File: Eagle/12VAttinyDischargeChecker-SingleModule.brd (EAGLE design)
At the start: 121.6 x 70.4 mm, 82 parts

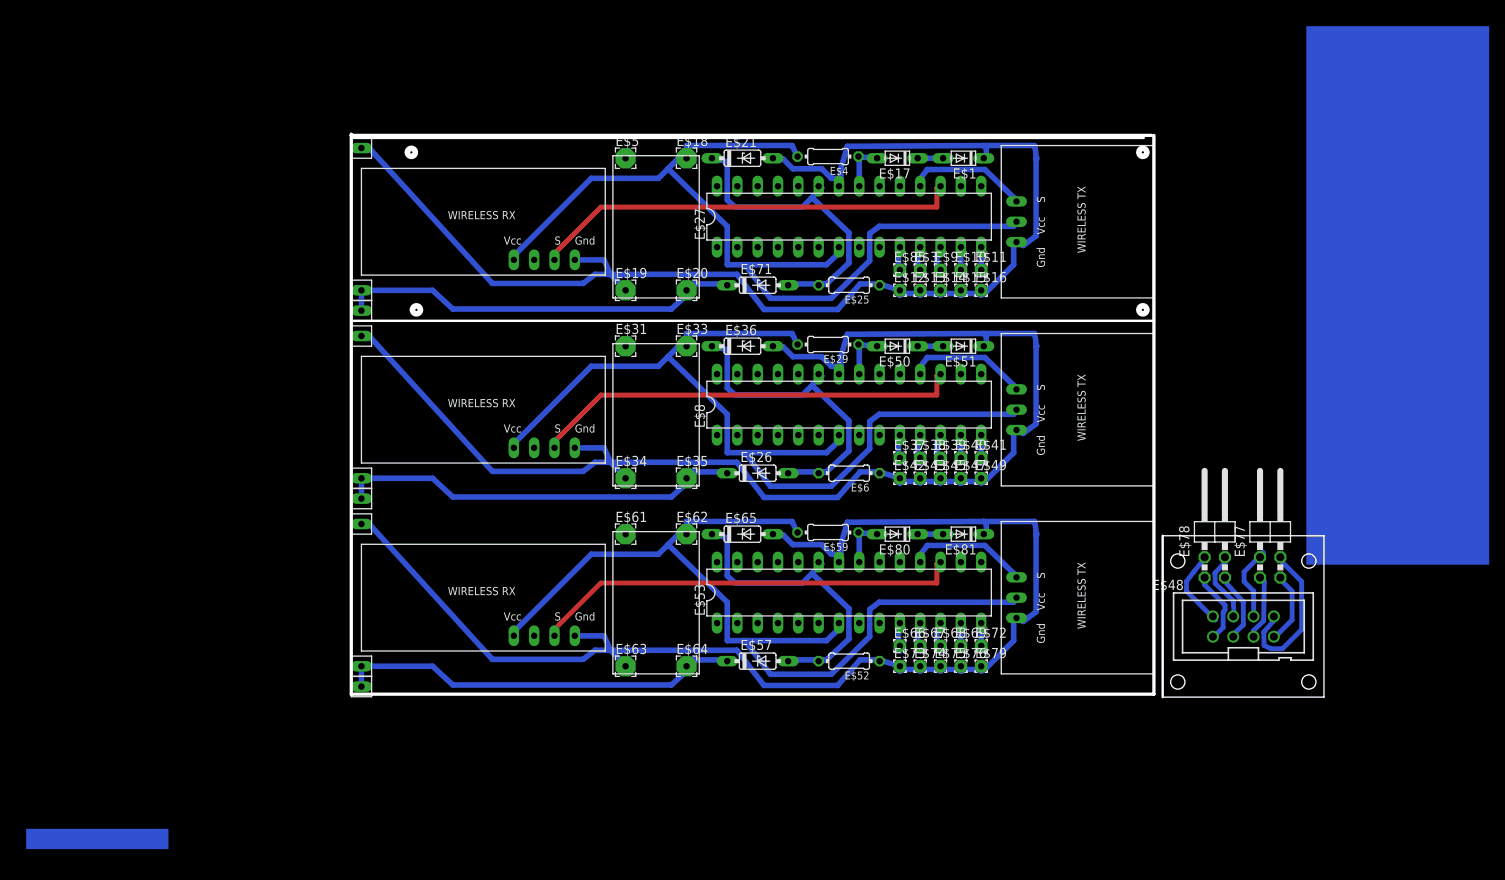
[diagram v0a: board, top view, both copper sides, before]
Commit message: Aggiunti file controllo e modifica al circuito single module per aggiungere debug e altre modifiche
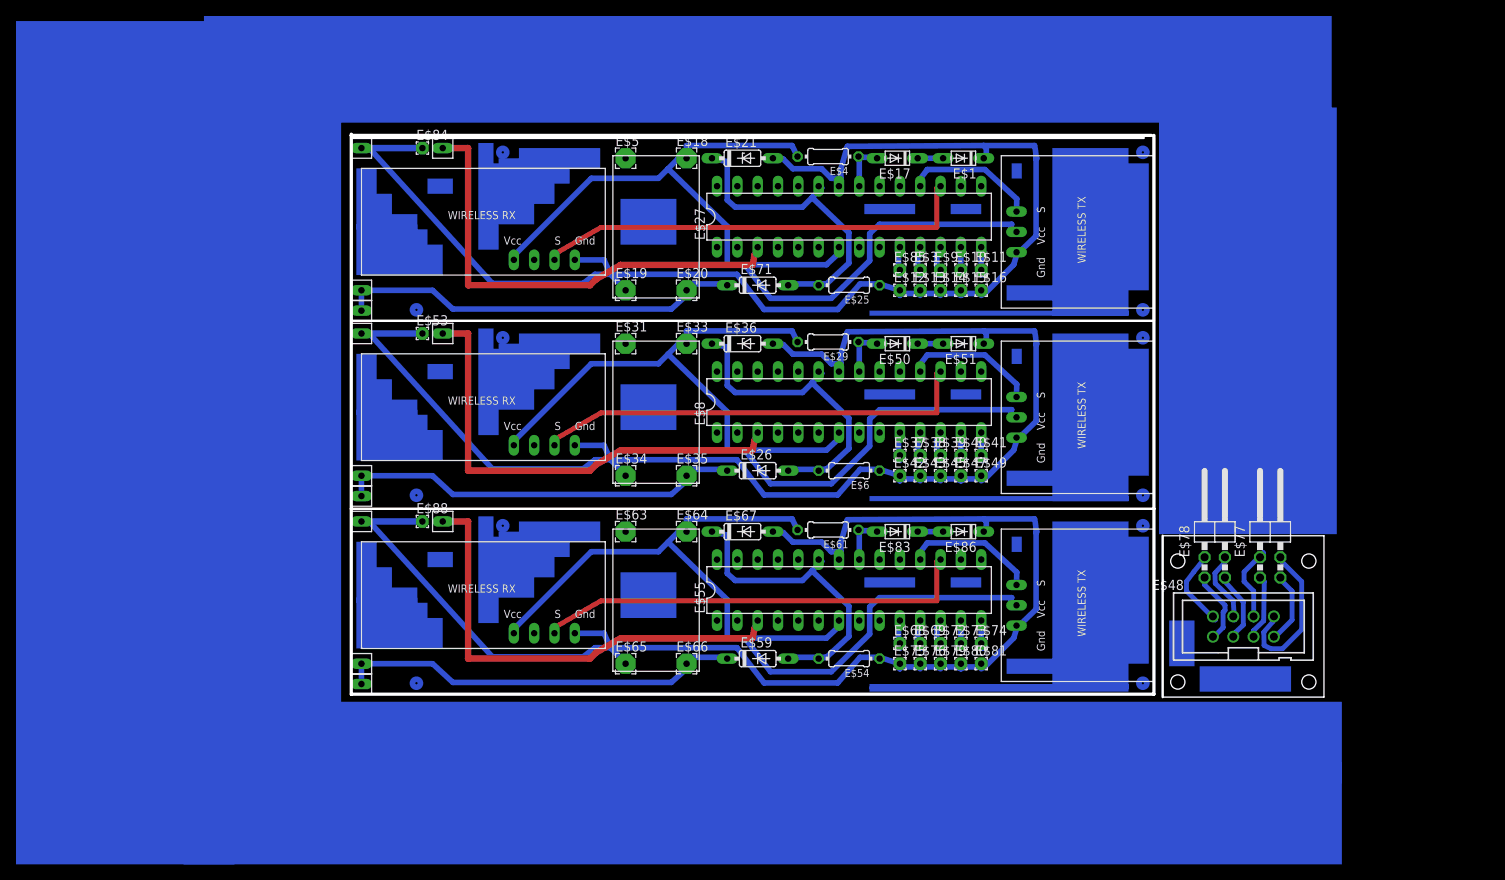
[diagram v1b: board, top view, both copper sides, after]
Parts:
- added E$82, E$87: (no value), con-lsta2:FE01-1
- added E$83, E$86: (no value), diode:DO34-5
- added E$84, E$88: (no value), wirepad:1,6/0,8
- E$52: value 220 -> (none); device eagle-ltspice:0204/7 -> con-lsta2:FE01-1
- E$53: device 74xx-us:DIL28-3 -> wirepad:1,6/0,8
- E$54: value (none) -> 220; device LSGPackages:WIRELESS-TX-FLAT -> eagle-ltspice:0204/7
- E$55: device con-lsta2:FE01-1 -> 74xx-us:DIL28-3
- E$56: device con-lsta2:FE01-1 -> LSGPackages:WIRELESS-TX-FLAT
- E$57: value Zener 12v -> (none); device ref-packages:DO35Z7 -> con-lsta2:FE01-1
- E$58: device LSGPackages:WIRELESS-RX-FLAT -> con-lsta2:FE01-1
- E$59: value 220 -> Zener 12v; device eagle-ltspice:0204/7 -> ref-packages:DO35Z7
- E$60: device con-lsta2:FE01-1 -> LSGPackages:WIRELESS-RX-FLAT
- E$61: value (none) -> 220; device wirepad:2,54/0,8 -> eagle-ltspice:0204/7
- E$62: device wirepad:2,54/0,8 -> con-lsta2:FE01-1
- E$65: value Zener 5v -> (none); device ref-packages:DO35Z7 -> wirepad:2,54/0,8
- E$66: device wirepad:1,6/0,8 -> wirepad:2,54/0,8
- E$67: value (none) -> Zener 5v; device wirepad:1,6/0,8 -> ref-packages:DO35Z7
- E$80, E$81: device diode:DO34-5 -> wirepad:1,6/0,8
- moved E$56 88.7 mm to (89.5, 12.1)
- moved E$52 64.5 mm to (11.4, 44.1), turned to 270 degrees
- moved E$53 62.4 mm to (8.89, 45.4)
- moved E$55 61.9 mm to (62.2, 13.3), turned to 0 degrees
- moved E$57 49.6 mm to (1.27, 2.86), turned to 90 degrees
- moved E$62 40.7 mm to (1.27, 23.2), turned to 90 degrees
- moved E$54 28.5 mm to (62.2, 4.76), turned to 180 degrees
- moved E$66 26.8 mm to (41.9, 4.13)
- moved E$67 26.4 mm to (48.9, 20.6)
- moved E$61 25.3 mm to (59.6, 20.8), turned to 180 degrees
- moved E$65 21.8 mm to (34.3, 4.13)
- moved E$58 19.2 mm to (1.27, 2.86), turned to 270 degrees
- moved E$59 18.1 mm to (50.8, 4.76), turned to 0 degrees
- moved E$80 18.0 mm to (76.2, 4.13), turned to 0 degrees
- moved E$60 17.2 mm to (16.5, 14.9), turned to 0 degrees
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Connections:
- new net S$42: E$27.3, E$82.1
- new net S$45: E$83.C, E$86.A
- new net S$46: E$55.3, E$87.1
- net S$18: now also E$53.1; no longer E$30.1
- net S$28: now also E$52.1, E$8.3; no longer E$53.7, E$54.P$1, E$58.P$1, E$59.2, E$62.1
- net S$29: now also E$55.7, E$56.P$1, E$60.P$1, E$61.2; no longer E$55.1, E$56.1, E$57.C
- net S$30: now also E$57.1, E$58.1, E$59.C, E$66.1; no longer E$52.2, E$53.23, E$57.A, E$65.C
- net S$31: now also E$54.2, E$55.23, E$59.A, E$67.C; no longer E$52.1, E$53.22, E$54.P$3, E$58.P$4, E$60.1, E$63.1, E$65.A, E$81.C
- net S$32: now also E$54.1, E$55.22, E$56.P$3, E$60.P$4, E$65.1, E$67.A, E$86.C, E$88.1; no longer E$53.18, E$54.P$2
- net S$33: now also E$55.18, E$56.P$2; no longer E$53.21, E$59.1, E$80.A
- net S$34: now also E$55.21, E$61.1, E$83.A; no longer E$53.17, E$58.P$3
- net S$35: now also E$55.17, E$60.P$3; no longer E$53.14
- net S$36: now also E$55.14; no longer E$53.13
- net S$37: now also E$84.1
- net S$38: now also E$55.13; no longer E$53.12
- net S$39: now also E$55.12; no longer E$53.11
- net S$40: now also E$55.11; no longer E$53.10
- net S$41: now also E$55.10; no longer E$80.C, E$81.A
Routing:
- net S$32: track 15.2 -> 169.5 mm
- net S$31: track 163.0 -> 40.1 mm
- net S$29: track 51.2 -> 116.1 mm
- net S$46: track 0.00 -> 59.0 mm
- net S$42: track 0.00 -> 59.0 mm
- net S$28: track 115.8 -> 59.0 mm
- net S$35: track 4.04 -> 55.0 mm
- net S$34: track 54.0 -> 6.01 mm
- net S$30: track 40.1 -> 51.2 mm
- net S$33: track 6.01 -> 16.6 mm
- net S$37: track 163.0 -> 169.5 mm
- net S$18: track 163.0 -> 169.5 mm
- net S$45: track 0.00 -> 3.18 mm
- net S$16: track 15.2 -> 16.6 mm
- net S$19: track 15.2 -> 16.6 mm
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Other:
- outline, holes or cut-outs redrawn
- board text added: "debug"

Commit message: .
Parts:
- removed E$22, E$56: (no value), LSGPackages:WIRELESS-TX-FLAT
- removed E$23, E$24, E$30, E$52, E$57, E$58, E$62, E$87: (no value), con-lsta2:FE01-1
- removed E$26, E$59: Zener 12v, ref-packages:DO35Z7
- removed E$28, E$60: (no value), LSGPackages:WIRELESS-RX-FLAT
- removed E$29, E$54, E$6, E$61: 220, eagle-ltspice:0204/7
- removed E$31, E$33, E$34, E$35, E$63, E$64, E$65, E$66: (no value), wirepad:2,54/0,8
- removed E$36, E$67: Zener 5v, ref-packages:DO35Z7
- removed E$37, E$38, E$39, E$40, E$41, E$42, E$43, E$45, E$47, E$49, E$53, E$68, E$69, E$72, E$73, E$74, E$75, E$76, E$79, E$80, E$81, E$88: (no value), wirepad:1,6/0,8
- removed E$50, E$51, E$83, E$86: (no value), diode:DO34-5
- removed E$55, E$8: (no value), 74xx-us:DIL28-3
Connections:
- removed net S$13: E$22.P$1, E$28.P$1, E$29.2, E$33.1, E$8.7
- removed net S$14: E$23.1, E$24.1, E$26.C, E$35.1
- removed net S$17: E$26.A, E$36.C, E$6.2, E$8.23
- removed net S$18: E$22.P$3, E$28.P$4, E$34.1, E$36.A, E$51.C, E$53.1, E$6.1, E$8.22
- removed net S$19: E$22.P$2, E$8.18
- removed net S$20: E$29.1, E$50.A, E$8.21
- removed net S$21: E$28.P$3, E$8.17
- removed net S$22: E$8.14
- removed net S$23: E$8.13
- removed net S$24: E$8.12
- removed net S$25: E$8.11
- removed net S$26: E$8.10
- removed net S$27: E$50.C, E$51.A
- removed net S$28: E$52.1, E$8.3
- removed net S$29: E$55.7, E$56.P$1, E$60.P$1, E$61.2, E$64.1
- removed net S$30: E$57.1, E$58.1, E$59.C, E$66.1
- removed net S$31: E$54.2, E$55.23, E$59.A, E$67.C
- removed net S$32: E$54.1, E$55.22, E$56.P$3, E$60.P$4, E$65.1, E$67.A, E$86.C, E$88.1
- removed net S$33: E$55.18, E$56.P$2
- removed net S$34: E$55.21, E$61.1, E$83.A
- removed net S$35: E$55.17, E$60.P$3
- removed net S$36: E$55.14
- removed net S$38: E$55.13
- removed net S$39: E$55.12
- removed net S$40: E$55.11
- removed net S$41: E$55.10
- removed net S$45: E$83.C, E$86.A
- removed net S$46: E$55.3, E$87.1
- new net S$47: E$27.6, E$85.1
- net S$15: now also E$27.20
- net S$37: now also E$27.8
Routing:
- net S$32: track 169.5 -> 0.00 mm
- net S$18: track 169.5 -> 0.00 mm
- net S$13: track 116.1 -> 0.00 mm
- net S$29: track 116.1 -> 0.00 mm
- net S$28: track 59.0 -> 0.00 mm
- net S$46: track 59.0 -> 0.00 mm
- net S$35: track 55.0 -> 0.00 mm
- net S$21: track 55.0 -> 0.00 mm
- net S$30: track 51.2 -> 0.00 mm
- net S$14: track 51.2 -> 0.00 mm
- net S$31: track 40.1 -> 0.00 mm
- net S$17: track 40.1 -> 0.00 mm
- net S$47: track 0.00 -> 18.5 mm
- net S$33: track 16.6 -> 0.00 mm
- net S$19: track 16.6 -> 0.00 mm
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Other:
- outline, holes or cut-outs redrawn

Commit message: .
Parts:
- added E$22: (no value), LSGPackages:WIRELESS-TX-FLAT
- added E$23, E$24, E$30, E$52: (no value), con-lsta2:FE01-1
- added E$26: Zener 12v, ref-packages:DO35Z7
- added E$28: (no value), LSGPackages:WIRELESS-RX-FLAT
- added E$29, E$6: 220, eagle-ltspice:0204/7
- added E$31, E$33, E$34, E$35: (no value), wirepad:2,54/0,8
- added E$36: Zener 5v, ref-packages:DO35Z7
- added E$37, E$38, E$39, E$40, E$41, E$42, E$43, E$45, E$47, E$49, E$53, E$54, E$55, E$56, E$57, E$58: (no value), wirepad:1,6/0,8
- added E$50, E$51: (no value), diode:DO34-5
- added E$8: (no value), 74xx-us:DIL28-3
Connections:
- new net S$13: E$22.P$1, E$28.P$1, E$29.2, E$33.1, E$8.20, E$8.7
- new net S$14: E$23.1, E$24.1, E$26.C, E$35.1
- new net S$17: E$26.A, E$36.C, E$6.2, E$8.23
- new net S$18: E$22.P$3, E$28.P$4, E$34.1, E$36.A, E$51.C, E$53.1, E$6.1, E$8.22, E$8.8
- new net S$19: E$22.P$2, E$56.1, E$8.18
- new net S$20: E$29.1, E$50.A, E$8.21
- new net S$21: E$28.P$3, E$57.1, E$8.17
- new net S$22: E$8.14
- new net S$23: E$8.13
- new net S$24: E$8.12
- new net S$25: E$8.11
- new net S$26: E$8.10
- new net S$27: E$50.C, E$51.A
- new net S$28: E$52.1, E$8.3
- new net S$29: E$37.1, E$8.6
- new net S$30: E$55.1, E$8.19
- new net S$31: E$54.1, E$8.1
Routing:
- net S$18: track 0.00 -> 175.2 mm
- net S$13: track 0.00 -> 128.1 mm
- net S$21: track 0.00 -> 108.9 mm
- net S$19: track 0.00 -> 68.8 mm
- net S$28: track 0.00 -> 59.2 mm
- net S$14: track 0.00 -> 51.2 mm
- net S$31: track 0.00 -> 44.1 mm
- net S$17: track 0.00 -> 40.1 mm
- net S$29: track 0.00 -> 16.4 mm
- net S$20: track 0.00 -> 6.01 mm
- net S$22: track 0.00 -> 4.04 mm
- net S$24: track 0.00 -> 3.97 mm
- net S$25: track 0.00 -> 3.78 mm
- net S$27: track 0.00 -> 3.17 mm
- net S$23: track 0.00 -> 2.86 mm
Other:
- outline, holes or cut-outs redrawn

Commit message: Prima di totale modifica
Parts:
- added E$59, E$66: 220, eagle-ltspice:0204/7
- added E$60: (no value), 74xx-us:DIL28-3
- added E$61: (no value), LSGPackages:WIRELESS-TX-FLAT
- added E$62, E$63, E$67, E$92: (no value), con-lsta2:FE01-1
- added E$64: Zener 12v, ref-packages:DO35Z7
- added E$65: (no value), LSGPackages:WIRELESS-RX-FLAT
- added E$68, E$69, E$72, E$73: (no value), wirepad:2,54/0,8
- added E$74: Zener 5v, ref-packages:DO35Z7
- added E$75, E$76, E$79, E$80, E$81, E$83, E$86, E$87, E$88, E$89, E$93, E$94, E$95, E$96, E$97, E$98: (no value), wirepad:1,6/0,8
- added E$90, E$91: (no value), diode:DO34-5
- moved E$28 2.54 mm to (16.7, 37.5)
- moved E$53 2.54 mm to (8.89, 44.5)
- moved E$54 2.54 mm to (20.3, 44.5)
- moved E$55 2.54 mm to (22.9, 44.5)
- moved E$56 2.54 mm to (25.4, 44.5)
- moved E$57 2.54 mm to (27.9, 44.5)
- moved E$58 2.54 mm to (6.35, 44.5)
- moved E$34 2.54 mm to (34.4, 26.7)
- moved E$35 2.54 mm to (42.1, 26.7)
- moved E$42 2.54 mm to (68.7, 26.7)
- moved E$43 2.54 mm to (71.3, 26.7)
- moved E$45 2.54 mm to (73.8, 26.7)
- moved E$47 2.54 mm to (76.4, 26.7)
- moved E$49 2.54 mm to (78.9, 26.7)
- moved E$22 2.54 mm to (89.7, 34.7)
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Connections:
- new net S$32: E$60.20, E$60.7, E$61.P$1, E$65.P$1, E$66.2, E$69.1
- new net S$33: E$62.1, E$63.1, E$64.C, E$73.1
- new net S$34: E$59.2, E$60.23, E$64.A, E$74.C
- new net S$35: E$59.1, E$60.22, E$60.8, E$61.P$3, E$65.P$4, E$67.1, E$72.1, E$74.A, E$83.1, E$86.1, E$87.1, E$88.1, E$89.1, E$91.C, E$93.1, E$98.1
- new net S$36: E$60.18, E$61.P$2, E$97.1
- new net S$38: E$60.21, E$66.1, E$90.A
- new net S$39: E$60.17, E$65.P$3, E$95.1
- new net S$40: E$60.14, E$81.1
- new net S$41: E$60.13, E$80.1
- new net S$45: E$60.12, E$79.1
- new net S$46: E$60.11, E$76.1
- new net S$48: E$60.10
- new net S$49: E$90.C, E$91.A
- new net S$50: E$60.3, E$92.1
- new net S$57: E$60.6, E$75.1
- new net S$58: E$60.1, E$94.1
- new net S$59: E$60.19, E$96.1
- net S$19: now also E$57.1; no longer E$56.1
- net S$21: now also E$55.1; no longer E$57.1
- net S$30: now also E$56.1; no longer E$55.1
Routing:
- net S$35: track 0.00 -> 214.6 mm
- net S$32: track 0.00 -> 139.8 mm
- net S$39: track 0.00 -> 88.4 mm
- net S$36: track 0.00 -> 66.7 mm
- net S$58: track 0.00 -> 58.3 mm
- net S$30: track 0.00 -> 53.2 mm
- net S$33: track 0.00 -> 51.4 mm
- net S$59: track 0.00 -> 49.7 mm
- net S$50: track 0.00 -> 46.7 mm
- net S$21: track 108.9 -> 70.2 mm
- net S$34: track 0.00 -> 37.9 mm
- net S$57: track 0.00 -> 11.4 mm
- net S$38: track 0.00 -> 6.22 mm
- net S$49: track 0.00 -> 3.60 mm
- net S$41: track 0.00 -> 3.14 mm
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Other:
- outline, holes or cut-outs redrawn

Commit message: Ultime modifiche
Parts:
- removed E$59, E$66: 220, eagle-ltspice:0204/7
- removed E$62, E$63, E$67, E$92: (no value), con-lsta2:FE01-1
- removed E$64: Zener 12v, ref-packages:DO35Z7
- removed E$65: (no value), LSGPackages:WIRELESS-RX-FLAT
- removed E$68, E$69, E$72, E$73: (no value), wirepad:2,54/0,8
- removed E$74: Zener 5v, ref-packages:DO35Z7
- removed E$75, E$76, E$79, E$80, E$81, E$83, E$84, E$86, E$87, E$88, E$89, E$93, E$94, E$95, E$96, E$97, E$98: (no value), wirepad:1,6/0,8
- removed E$90, E$91: (no value), diode:DO34-5
- added E$104: (no value), con-usb-3:USB-MB-H
- E$1: value (none) -> 220; device diode:DO34-5 -> eagle-ltspice:0204/7
- E$10, E$11, E$12, E$13, E$43, E$45: device wirepad:1,6/0,8 -> wirepad:2,54/0,8
- E$14, E$47: value (none) -> Zener 5v; device wirepad:1,6/0,8 -> ref-packages:DO35Z7
- E$17, E$50, E$51: device diode:DO34-5 -> wirepad:1,6/0,8
- E$18, E$19, E$20, E$31, E$33: device wirepad:2,54/0,8 -> wirepad:1,6/0,8
- E$2: device LSGPackages:WIRELESS-RX-FLAT -> 74xx-us:DIL28-3
- E$21: value Zener 5v -> (none); device ref-packages:DO35Z7 -> wirepad:1,6/0,8
- E$22, E$32: device LSGPackages:WIRELESS-TX-FLAT -> wirepad:1,6/0,8
- E$23, E$24, E$30, E$52: device con-lsta2:FE01-1 -> wirepad:1,6/0,8
- E$25: value 220 -> (none); device eagle-ltspice:0204/7 -> diode:DO34-5
- E$26, E$71: value Zener 12v -> (none); device ref-packages:DO35Z7 -> diode:DO34-5
- E$27: device 74xx-us:DIL28-3 -> con-lsta2:FE01-1
- E$28: device LSGPackages:WIRELESS-RX-FLAT -> wirepad:1,6/0,8
- E$29: value 220 -> (none); device eagle-ltspice:0204/7 -> wirepad:1,6/0,8
- E$3: device wirepad:1,6/0,8 -> LSGPackages:WIRELESS-TX-FLAT
- E$34: value (none) -> 220; device wirepad:2,54/0,8 -> eagle-ltspice:0204/7
- E$35: device wirepad:2,54/0,8 -> 74xx-us:DIL28-3
- E$36: value Zener 5v -> (none); device ref-packages:DO35Z7 -> LSGPackages:WIRELESS-TX-FLAT
- E$37, E$38, E$42, E$9: device wirepad:1,6/0,8 -> con-lsta2:FE01-1
- E$39: value (none) -> Zener 12v; device wirepad:1,6/0,8 -> ref-packages:DO35Z7
- E$4: value 220 -> (none); device eagle-ltspice:0204/7 -> con-lsta2:FE01-1
- E$40: device wirepad:1,6/0,8 -> LSGPackages:WIRELESS-RX-FLAT
- E$41: value (none) -> 220; device wirepad:1,6/0,8 -> eagle-ltspice:0204/7
- E$44, E$46: device con-lsta2:FE01-1 -> wirepad:2,54/0,8
- E$5: device wirepad:2,54/0,8 -> con-lsta2:FE01-1
- E$6: value 220 -> Zener 12v; device eagle-ltspice:0204/7 -> ref-packages:DO35Z7
- E$60: value (none) -> 10k; device 74xx-us:DIL28-3 -> eagle-ltspice:0204/7
- E$61: device LSGPackages:WIRELESS-TX-FLAT -> resistor:C050-024X044
- E$7: device con-lsta2:FE01-1 -> LSGPackages:WIRELESS-RX-FLAT
- E$8: value (none) -> 220; device 74xx-us:DIL28-3 -> eagle-ltspice:0204/7
- E$82: device con-lsta2:FE01-1 -> diode:DO34-5
- moved E$61 90.7 mm to (18.7, 68.3), turned to 0 degrees
- moved E$42 79.8 mm to (1.42, 69.6), turned to 90 degrees
- moved E$24 77.2 mm to (78.6, 26.8), turned to 0 degrees
- moved E$23 74.6 mm to (76.1, 26.8), turned to 0 degrees
- moved E$9 72.9 mm to (1.13, 45.8), turned to 90 degrees
- moved E$58 72.8 mm to (78.9, 50.5)
- moved E$38 72.7 mm to (1.42, 49.3), turned to 270 degrees
- moved E$4 72.0 mm to (1.13, 25.5), turned to 90 degrees
- moved E$53 70.5 mm to (78.9, 53.1)
- moved E$37 70.2 mm to (1.42, 49.3), turned to 90 degrees
- moved E$40 67.8 mm to (16.7, 61.3)
- moved E$52 65.7 mm to (76.4, 53.1), turned to 0 degrees
- moved E$85 65.5 mm to (4.76, 68.3)
- moved E$60 65.5 mm to (27.0, 68.2), turned to 180 degrees
- moved E$82 65.2 mm to (76.7, 67.0), turned to 180 degrees
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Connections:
- removed net S$35: E$59.1, E$60.22, E$60.8, E$61.P$3, E$65.P$4, E$67.1, E$72.1, E$74.A, E$83.1, E$86.1, E$87.1, E$88.1, E$89.1, E$91.C, E$93.1, E$98.1
- removed net S$36: E$60.18, E$61.P$2, E$97.1
- removed net S$38: E$60.21, E$66.1, E$90.A
- removed net S$39: E$60.17, E$65.P$3, E$95.1
- removed net S$40: E$60.14, E$81.1
- removed net S$41: E$60.13, E$80.1
- removed net S$42: E$27.3, E$82.1
- removed net S$45: E$60.12, E$79.1
- removed net S$46: E$60.11, E$76.1
- removed net S$48: E$60.10
- removed net S$49: E$90.C, E$91.A
- removed net S$50: E$60.3, E$92.1
- removed net S$57: E$60.6, E$75.1
- removed net S$58: E$60.1, E$94.1
- removed net S$59: E$60.19, E$96.1
- net S$10: now also E$19.1, E$2.14; no longer E$27.12
- net S$11: now also E$18.1, E$2.13; no longer E$27.11
- net S$12: now also E$17.1, E$2.12; no longer E$27.10
- net S$13: now also E$16.1, E$2.11; no longer E$22.P$1, E$28.P$1, E$29.2, E$33.1, E$8.20, E$8.7
- net S$14: now also E$2.10; no longer E$23.1, E$24.1, E$26.C, E$35.1
- net S$15: now also E$25.C, E$26.A; no longer E$18.1, E$2.P$1, E$27.20, E$27.7, E$32.P$1, E$4.2
- net S$16: now also E$2.3, E$27.1; no longer E$27.18, E$32.P$2
- net S$17: now also E$15.1, E$2.6; no longer E$26.A, E$36.C, E$6.2, E$8.23
- net S$18: now also E$2.1, E$29.1; no longer E$22.P$3, E$28.P$4, E$34.1, E$36.A, E$51.C, E$53.1, E$6.1, E$8.22, E$8.8
- net S$19: now also E$2.19, E$31.1; no longer E$22.P$2, E$57.1, E$8.18
- net S$2: now also E$11.1, E$2.20, E$2.7, E$3.P$1, E$7.P$1, E$8.2; no longer E$20.1, E$44.1, E$46.1, E$71.C
- net S$20: now also E$35.20, E$35.7, E$36.P$1, E$40.P$1, E$41.2, E$44.1, E$60.1; no longer E$29.1, E$50.A, E$8.21
- net S$21: now also E$37.1, E$38.1, E$39.C, E$46.1; no longer E$28.P$3, E$55.1, E$8.17
- net S$22: now also E$34.2, E$35.23, E$39.A, E$47.C; no longer E$8.14
- net S$23: now also E$104.P$7, E$34.1, E$35.22, E$35.8, E$36.P$3, E$40.P$4, E$42.1, E$45.1, E$47.A, E$54.1, E$55.1, E$56.1, E$57.1, E$58.1, E$82.C, E$85.1; no longer E$8.13
- net S$24: now also E$35.18, E$36.P$2; no longer E$8.12
- net S$25: now also E$35.21, E$41.1, E$71.A; no longer E$8.11
- net S$26: now also E$35.1, E$60.2, E$61.2; no longer E$8.10
- net S$27: now also E$35.14, E$53.1; no longer E$50.C, E$51.A
- net S$28: now also E$35.13; no longer E$8.3
- net S$29: now also E$35.12, E$51.1; no longer E$37.1, E$8.6
- net S$3: now also E$13.1, E$4.1, E$5.1, E$6.C; no longer E$27.14
- net S$30: now also E$35.11, E$50.1; no longer E$56.1, E$8.19
- net S$31: now also E$35.10; no longer E$54.1, E$8.1
- net S$32: now also E$104.D-, E$35.3; no longer E$60.20, E$60.7, E$61.P$1, E$65.P$1, E$66.2, E$69.1
- net S$33: now also E$104.D+, E$35.2; no longer E$62.1, E$63.1, E$64.C, E$73.1
- net S$34: now also E$104.ID, E$61.1; no longer E$59.2, E$60.23, E$64.A, E$74.C
- net S$37: now also E$71.C, E$82.A; no longer E$1.C, E$19.1, E$2.P$4, E$21.A, E$25.1, E$27.22, E$27.8, E$32.P$3, E$7.1, E$84.1
- net S$4: now also E$1.2, E$14.C, E$2.23, E$6.A; no longer E$17.A, E$27.21, E$4.1
- net S$47: now also E$35.6, E$49.1; no longer E$27.6, E$85.1
- net S$5: now also E$1.1, E$12.1, E$14.A, E$2.22, E$2.8, E$20.1, E$21.1, E$22.1, E$23.1, E$24.1, E$26.C, E$28.1, E$3.P$3, E$33.1, E$7.P$4; no longer E$1.A, E$17.C
- net S$7: now also E$2.18, E$3.P$2, E$32.1; no longer E$21.C, E$25.2, E$27.23, E$71.A
- net S$8: now also E$2.21, E$25.A, E$8.1; no longer E$27.13
- net S$9: now also E$2.17, E$30.1, E$7.P$3; no longer E$2.P$3, E$27.17
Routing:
- net S$35: track 214.6 -> 0.00 mm
- net S$5: track 3.18 -> 216.0 mm
- net S$23: track 2.86 -> 215.6 mm
- net S$37: track 175.4 -> 3.60 mm
- net S$20: track 6.01 -> 153.6 mm
- net S$13: track 128.1 -> 3.04 mm
- net S$15: track 128.1 -> 3.60 mm
- net S$18: track 175.2 -> 58.9 mm
- net S$2: track 51.2 -> 139.8 mm
- net S$39: track 88.4 -> 0.00 mm
- net S$32: track 139.8 -> 54.5 mm
- net S$36: track 66.7 -> 0.00 mm
- net S$42: track 59.0 -> 0.00 mm
- net S$58: track 58.3 -> 0.00 mm
- net S$28: track 59.2 -> 3.14 mm
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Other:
- board text added: "Mosi"
- board text added: "mi"
- board text added: "mo"
- board text added: "rs"
- board text added: "sck"

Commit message: .
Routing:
- net S$23: track 215.6 -> 148.6 mm
- net S$20: track 153.6 -> 87.6 mm
- net S$33: track 88.7 -> 43.5 mm
- net S$26: track 27.7 -> 49.9 mm
- net S$22: track 37.9 -> 33.6 mm
- net S$32: track 54.5 -> 56.4 mm
- net S$34: track 21.4 -> 19.8 mm
- net S$21: track 52.7 -> 51.2 mm
- net S$28: track 3.14 -> 3.78 mm
